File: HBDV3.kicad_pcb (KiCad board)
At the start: 2 copper layers, 56 parts, among them J1 RJ45 PWR, J2 Screw_Terminal_01x02 PWR, J3 RJ45 IN, J4 RJ45 OUT, J5 push_Terminal_01x04, J6 push_Terminal_01x04

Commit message: Changed diode, rough PCB layout
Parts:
- added H1: MountingHole, MountingHole:MountingHole_4.3mm_M4_DIN965, F.Cu at (165.0, 57.5)
- added H2: MountingHole, MountingHole:MountingHole_4.3mm_M4_DIN965, F.Cu at (225.0, 57.5)
- added H3: MountingHole, MountingHole:MountingHole_4.3mm_M4_DIN965, F.Cu at (211.0, 85.8)
- added H4: MountingHole, MountingHole:MountingHole_4.3mm_M4_DIN965, F.Cu at (251.0, 85.8)
- added J2: RJ45 PWR, Library:RJ45_E5J8800LJG2L, F.Cu at (150.8, 83.6)
- D1, D2, D3, D6, D7, D8: value QH05BZ600 -> PMEG10020ELRX; footprint Package_TO_SOT_SMD:TO-263-2 -> Diode_SMD:Nexperia_CFP3_SOD-123W
- moved J1 178.2 mm to (269.4, 88.3), turned to 90 degrees
- moved D7 174.7 mm to (250.1, 68.2)
- moved J4 174.7 mm to (269.1, 61.9), turned to 180 degrees
- moved D8 157.7 mm to (234.9, 93.7), turned to -90 degrees
- moved D6 152.2 mm to (229.8, 72.5)
- moved C8 137.9 mm to (275.8, 75.0), turned to 180 degrees
- moved C9 137.5 mm to (269.2, 72.8), turned to -90 degrees
- moved R24 135.6 mm to (266.2, 75.0), turned to 90 degrees
- moved R21 133.4 mm to (257.8, 74.8), turned to 90 degrees
- moved R18 132.4 mm to (242.2, 74.8), turned to 90 degrees
- moved R20 127.7 mm to (252.8, 74.8), turned to 90 degrees
- moved R17 124.3 mm to (236.8, 79.0), turned to 90 degrees
- moved R19 121.7 mm to (247.5, 74.8), turned to 90 degrees
- moved D10 118.9 mm to (262.5, 75.0), turned to 90 degrees
- moved R16 118.2 mm to (231.8, 79.0), turned to 90 degrees
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- renumbered J2 to J3, J3 to J4, J4 to J5, J5 to J6, J6 to J7
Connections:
- D1 pad 1: /VDDA -> Net-(D1-K)
- D1 pad 2: unconnected-(D1-NC-Pad2) -> /VOUTA
- D2 pad 1: Net-(D2-C) -> Net-(D2-K)
- D2 pad 2: unconnected-(D2-NC-Pad2) -> /VOUTB
- D3 pad 1: Net-(D3-C) -> /VDDA
- D3 pad 2: unconnected-(D3-NC-Pad2) -> Net-(D3-A)
- D6 pad 1: /VDDA_B -> Net-(D6-K)
- D6 pad 2: unconnected-(D6-NC-Pad2) -> /VOUTA_B
- D7 pad 1: Net-(D7-C) -> Net-(D7-K)
- D7 pad 2: unconnected-(D7-NC-Pad2) -> /VOUTB_B
- D8 pad 1: Net-(D8-C) -> /VDDA_B
- D8 pad 2: unconnected-(D8-NC-Pad2) -> Net-(D8-A)
- R10 pad 2: Net-(D1-A) -> Net-(D3-A)
- R14 pad 2: Net-(D7-C) -> Net-(D6-K)
- R15 pad 2: Net-(D7-C) -> Net-(D6-K)
- R18 pad 2: Net-(D8-C) -> Net-(D7-K)
- R19 pad 2: Net-(D8-C) -> Net-(D7-K)
- R2 pad 2: Net-(D2-C) -> Net-(D1-K)
- R22 pad 2: Net-(D6-A) -> Net-(D8-A)
- R3 pad 2: Net-(D2-C) -> Net-(D1-K)
- R6 pad 2: Net-(D3-C) -> Net-(D2-K)
- R7 pad 2: Net-(D3-C) -> Net-(D2-K)
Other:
- board outline added: 137 x 45 mm

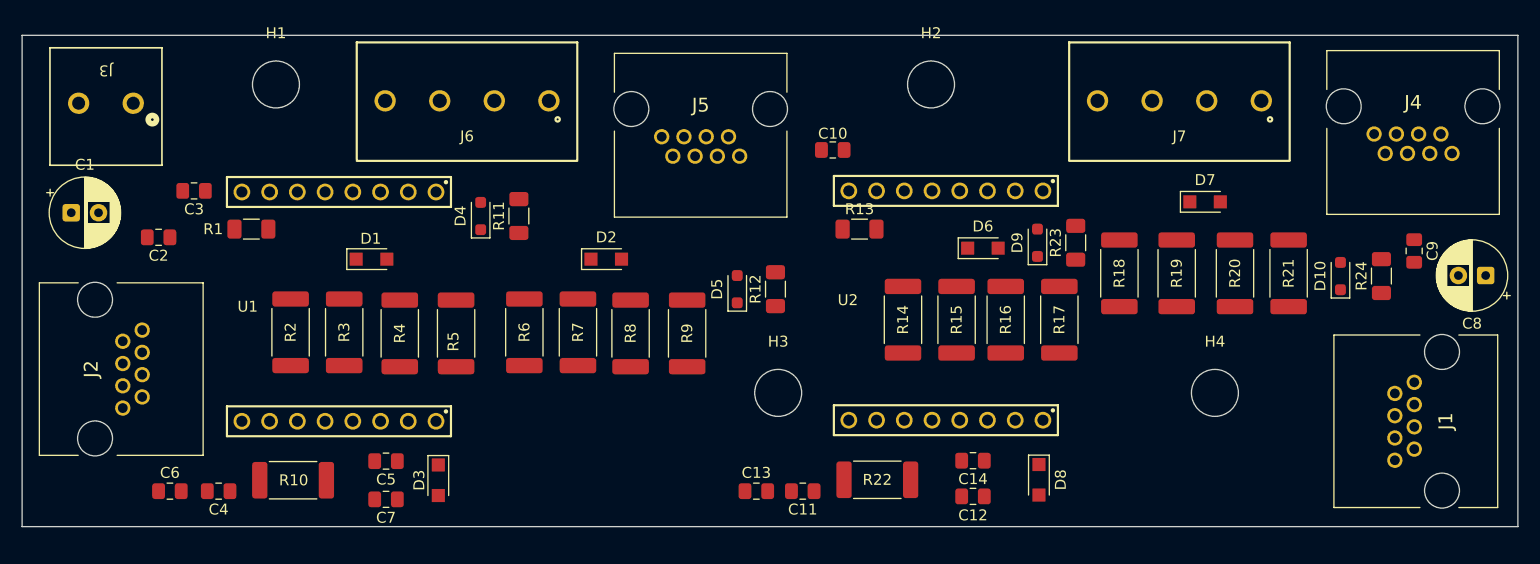
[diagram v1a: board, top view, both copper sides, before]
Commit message: Finished layout, added silkscreen text, configured track width
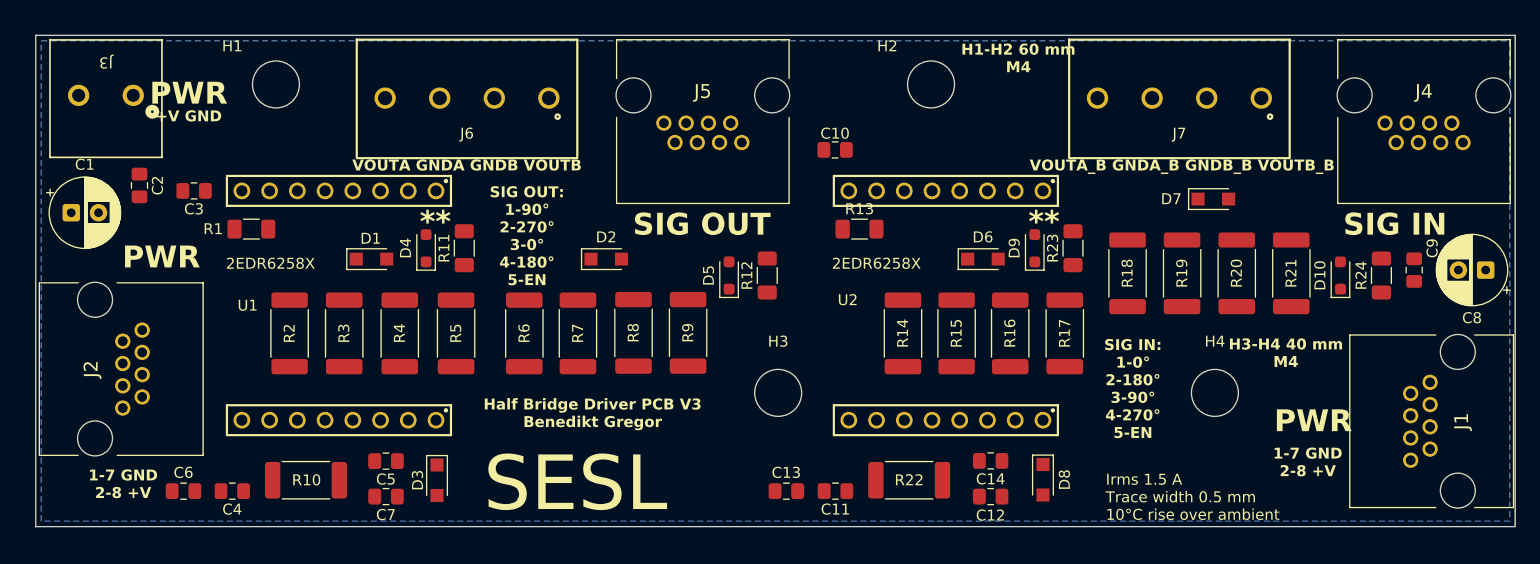
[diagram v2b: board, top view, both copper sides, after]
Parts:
- moved D4 5.81 mm to (178.8, 72.5)
- moved R11 5.81 mm to (182.2, 72.5)
- moved C2 5.06 mm to (152.5, 66.8), turned to -90 degrees
- moved C11 3.00 mm to (216.2, 94.8)
- moved R22 2.92 mm to (223.0, 93.8)
- moved C13 2.75 mm to (211.8, 94.8)
- moved C9 1.75 mm to (269.2, 74.5)
- moved C12 1.62 mm to (230.5, 95.2)
- moved C14 1.62 mm to (230.5, 92.0)
- moved D5 1.46 mm to (206.5, 75.0)
- moved R12 1.46 mm to (210.0, 75.0)
- moved J1 1.45 mm to (270.9, 88.3)
- moved J4 1.41 mm to (270.1, 60.9)
- moved R17 1.35 mm to (237.2, 80.3)
- moved R16 1.32 mm to (232.2, 80.3)
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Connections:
- net Net-(U1-STP/DTC) renamed /STP U1
- net Net-(U2-STP/DTC) renamed /STP U2
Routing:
- added copper zone on B.Cu, net GND
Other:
- board size 137 x 45 mm -> 135.5 x 45 mm
- board text added: "**"
- board text added: "+V GND"
- board text added: "1-7 GND 2-8 +V"
- board text added: "2EDR6258X"
- board text added: "H1-H2 60 mm M4"
- board text added: "H3-H4 40 mm M4"
- board text added: "Half Bridge Driver PCB V3 Benedikt Gregor"
- board text added: "Irms 1.5 A Trace width 0.5 mm 10°C rise over ambient"
- board text added: "PWR"
- board text added: "SESL"
- board text added: "SIG IN"
- board text added: "SIG IN: 1-0° 2-180° 3-90° 4-270° 5-EN"
- board text added: "SIG OUT"
- board text added: "SIG OUT: 1-90° 2-270° 3-0° 4-180° 5-EN"
- board text added: "VOUTA GNDA GNDB VOUTB"
- board text added: "VOUTA_B GNDA_B GNDB_B VOUTB_B"

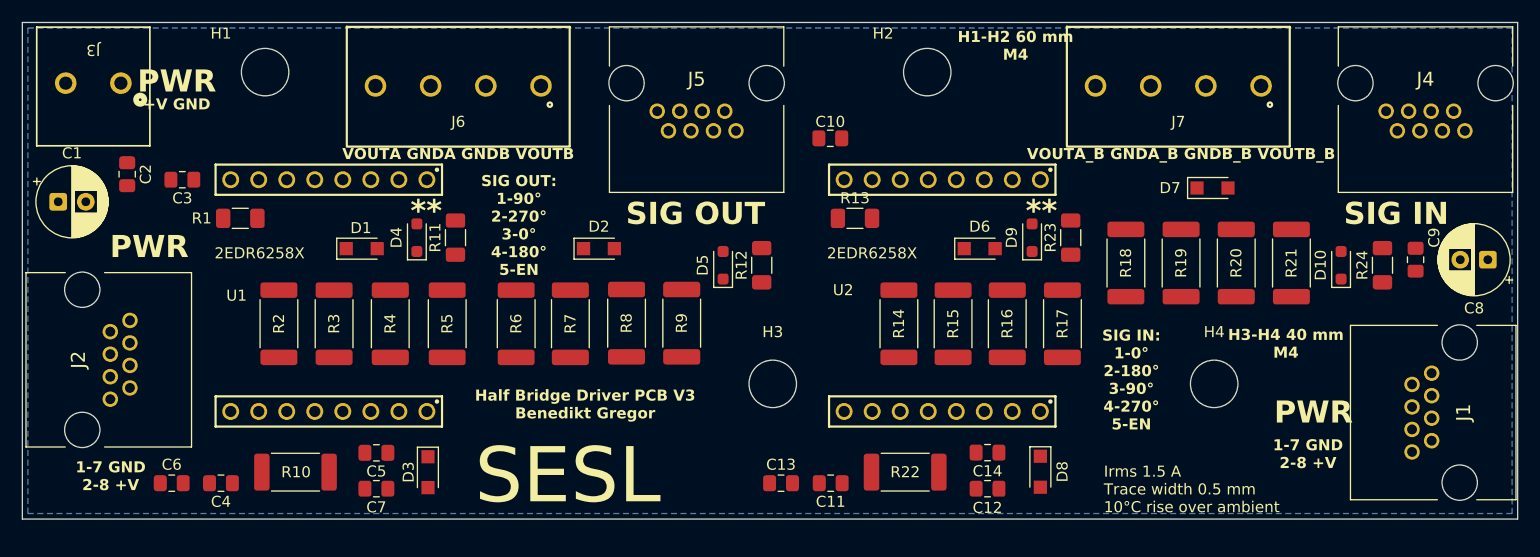
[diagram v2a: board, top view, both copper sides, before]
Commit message: Finished PCB routing
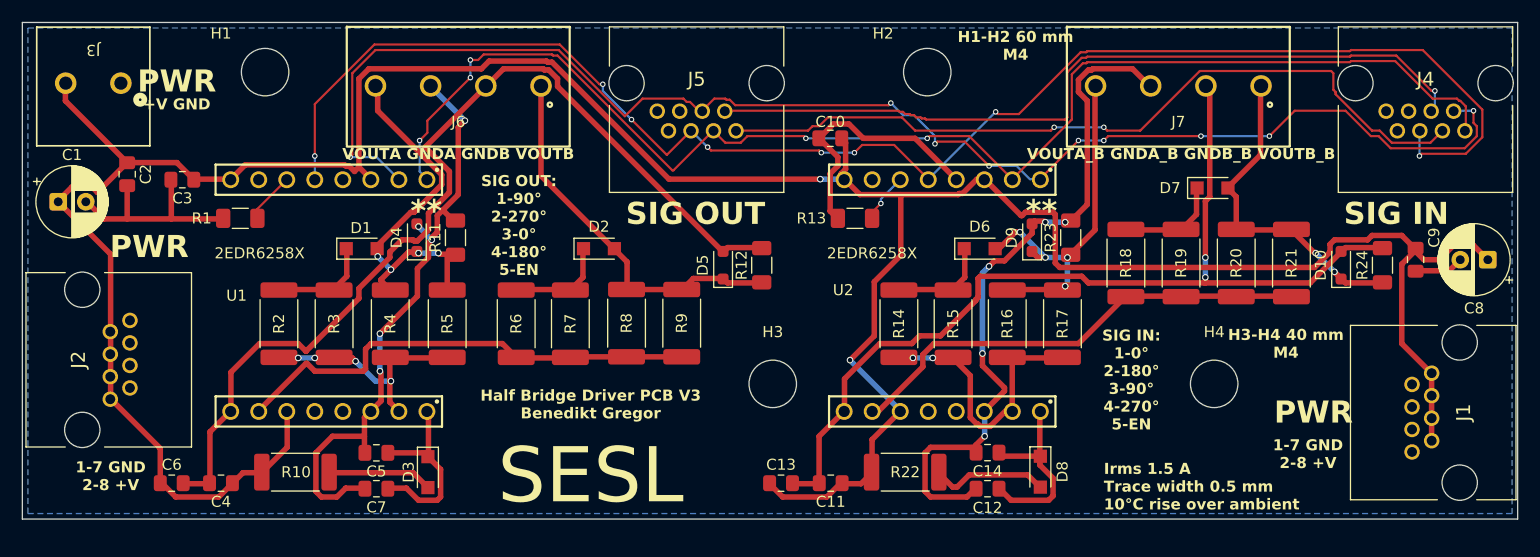
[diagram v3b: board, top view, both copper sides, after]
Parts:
- added G***: LOGO, LOGO, B.Cu at (193.5, 76.8)
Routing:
- net +16.5V: track 0.00 -> 279.1 mm, vias 0 -> 2
- net /ENABLE: track 0.00 -> 141.1 mm, vias 0 -> 8
- net Phase 180: track 0.00 -> 131.9 mm, vias 0 -> 9
- net Phase 0: track 0.00 -> 122.4 mm, vias 0 -> 5
- net /GNDB: track 0.00 -> 88.3 mm
- net /GNDB_B: track 0.00 -> 86.4 mm, vias 0 -> 2
- net Phase 270: track 0.00 -> 72.8 mm, vias 0 -> 1
- net Phase 90: track 0.00 -> 71.6 mm, vias 0 -> 2
- net /GNDA_B: track 0.00 -> 63.5 mm, vias 0 -> 5
- net /GNDA: track 0.00 -> 55.3 mm, vias 0 -> 5
- net GND: track 0.00 -> 48.2 mm
- net /OUTB: track 0.00 -> 43.4 mm
- net /OUTB_B: track 0.00 -> 43.2 mm
- net /VOUTB: track 0.00 -> 34.7 mm
- net /VOUTA_B: track 0.00 -> 34.4 mm, vias 0 -> 4
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
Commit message: Updated sig in/out for phase splitter compatibility + zener series R
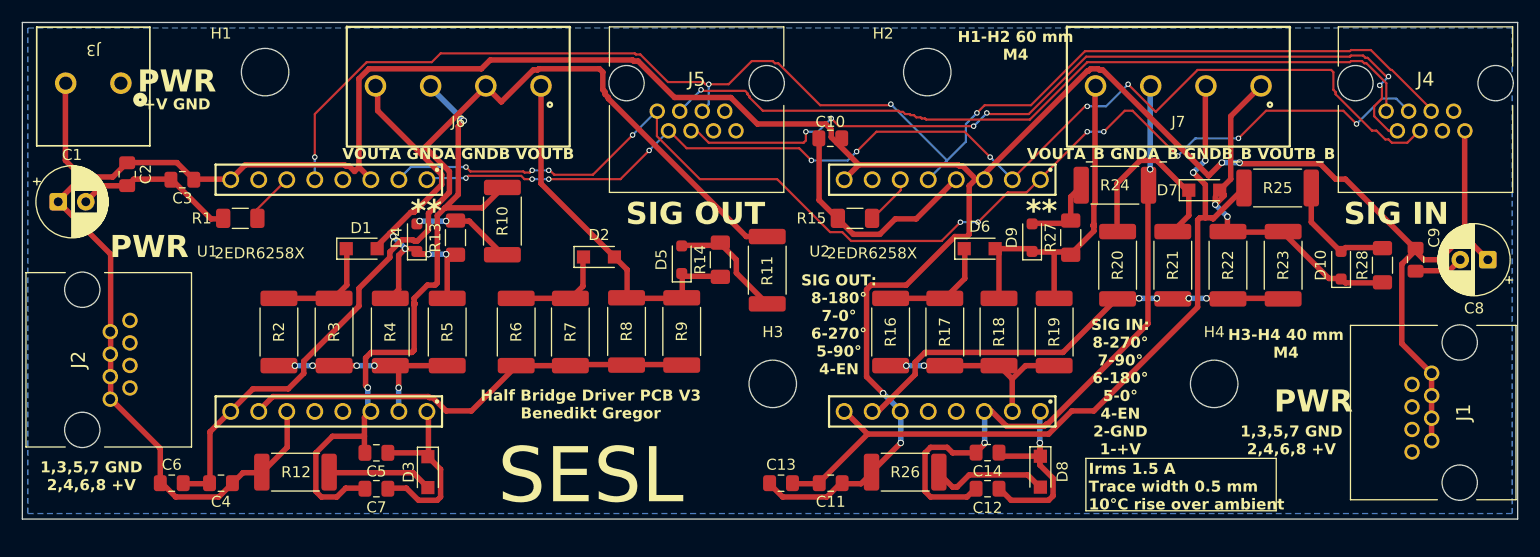
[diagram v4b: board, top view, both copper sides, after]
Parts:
- added R10: 2, Resistor_SMD:R_2512_6332Metric_Pad1.40x3.35mm_HandSolder, F.Cu at (186.5, 71.0)
- added R11: 2, Resistor_SMD:R_2512_6332Metric_Pad1.40x3.35mm_HandSolder, F.Cu at (210.5, 75.5)
- added R24: 2, Resistor_SMD:R_2512_6332Metric_Pad1.40x3.35mm_HandSolder, F.Cu at (242.0, 67.8)
- added R25: 2, Resistor_SMD:R_2512_6332Metric_Pad1.40x3.35mm_HandSolder, F.Cu at (256.8, 68.0)
- moved D5 3.78 mm to (202.8, 74.5)
- moved R14 3.78 mm to (206.2, 74.5)
- moved R16 1.06 mm to (221.7, 81.0)
- moved R17 1.06 mm to (226.6, 81.0)
- moved R18 1.06 mm to (231.5, 81.0)
- moved R19 1.06 mm to (236.5, 81.0)
- moved D7 0.78 mm to (250.1, 68.2)
- moved R20 0.78 mm to (242.2, 75.0)
- moved R21 0.78 mm to (247.2, 75.0)
- moved R22 0.78 mm to (252.2, 75.0)
- moved R23 0.78 mm to (257.2, 75.0)
- moved D2 0.75 mm to (195.2, 74.2)
- moved R2 0.75 mm to (166.2, 81.0)
- moved R3 0.75 mm to (171.2, 81.0)
- moved R4 0.75 mm to (176.3, 81.0)
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- renumbered R10 to R12, R11 to R13, R12 to R14, R13 to R15, R14 to R16, R15 to R17, R16 to R18, R17 to R19, R18 to R20, R19 to R21, R20 to R22, R21 to R23, R22 to R26, R23 to R27, R24 to R28
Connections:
- D10 pad 2: /GNDB_B -> Net-(D10-A)
- D4 pad 2: /GNDA -> Net-(D4-A)
- D5 pad 2: /GNDB -> Net-(D5-A)
- D9 pad 2: /GNDA_B -> Net-(D9-A)
- J4 pad 1: Phase 0 -> +16.5V
- J4 pad 2: Phase 180 -> GND
- J4 pad 3: Phase 90 -> unconnected-(J4-Pad3)
- J4 pad 4: Phase 270 -> /ENABLE
- J4 pad 5: /ENABLE -> Phase 0
- J4 pad 6: unconnected-(J4-Pad6) -> Phase 180
- J4 pad 7: unconnected-(J4-Pad7) -> Phase 90
- J4 pad 8: unconnected-(J4-Pad8) -> Phase 270
- J5 pad 1: Phase 90 -> unconnected-(J5-Pad1)
- J5 pad 2: Phase 270 -> unconnected-(J5-Pad2)
- J5 pad 3: Phase 0 -> unconnected-(J5-Pad3)
- J5 pad 4: Phase 180 -> /ENABLE
- J5 pad 5: /ENABLE -> Phase 90
- J5 pad 6: unconnected-(J5-Pad6) -> Phase 270
- J5 pad 7: unconnected-(J5-Pad7) -> Phase 0
- J5 pad 8: unconnected-(J5-Pad8) -> Phase 180
- R13 pad 2: /GNDA -> Net-(D4-A)
- R14 pad 2: /GNDB -> Net-(D5-A)
- R27 pad 2: /GNDA_B -> Net-(D9-A)
- R28 pad 2: /GNDB_B -> Net-(D10-A)
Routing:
- net Phase 180: track 131.9 -> 111.1 mm, vias 9 -> 11
- net Phase 0: track 122.4 -> 106.2 mm, vias 5 -> 9
- net +16.5V: track 279.1 -> 294.8 mm, vias 2 -> 4
- net /GNDB_B: track 86.4 -> 72.7 mm
- net /ENABLE: track 141.1 -> 127.6 mm, vias 8 -> 4
- net Net-(D5-A): track 0.00 -> 10.9 mm
- net Net-(D10-A): track 0.00 -> 10.9 mm
- net Net-(D4-A): track 0.00 -> 9.22 mm, vias 0 -> 2
- net Net-(D7-K): track 9.53 -> 17.5 mm
- net Net-(D9-A): track 0.00 -> 7.37 mm
- net GND: track 48.2 -> 41.0 mm
- net /OUTA_B: track 26.1 -> 18.9 mm
- net /GNDA: track 55.3 -> 60.7 mm, vias 5 -> 2
- net /GNDA_B: track 63.5 -> 58.7 mm, vias 5 -> 2
- net Phase 90: track 71.6 -> 75.8 mm, vias 2 -> 6
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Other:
- board text added: "1,3,5,7 GND 2,4,6,8 +V"
- board text added: "SIG IN: 8-270° 7-90° 6-180° 5-0° 4-EN 2-GND 1-+V"
- board text added: "SIG OUT: 8-180° 7-0° 6-270° 5-90° 4-EN"
- board text removed: "1-7 GND 2-8 +V"
- board text removed: "SIG IN: 1-0° 2-180° 3-90° 4-270° 5-EN"
- board text removed: "SIG OUT: 1-90° 2-270° 3-0° 4-180° 5-EN"

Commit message: Gerber files and 4.7uF cap adjustment
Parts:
- C11, C12, C4, C5: value 2.2uF -> 4.7uF
- moved G*** 2.47 mm to (193.2, 79.2)
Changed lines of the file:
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@@
 			(plot_on_all_layers_selection 0x00000000_00000000_00000000_00000000)
 			(disableapertmacros no)
-			(usegerberextensions no)
+			(usegerberextensions yes)
 			(usegerberattributes yes)
 			(usegerberadvancedattributes yes)
-			(creategerberjobfile yes)
+			(creategerberjobfile no)
 			(dashed_line_dash_ratio 12)
 			(dashed_line_gap_ratio 3)
@@
 			(outputformat 1)
 			(mirror no)
-			(drillshape 1)
+			(drillshape 0)
 			(scaleselection 1)
-			(outputdirectory "")
+			(outputdirectory "Gerberfiles_jlc")
 		)
 	)
@@
 			)
 		)
-		(property "Value" "2.2uF"
+		(property "Value" "4.7uF"
 			(at 0 1.68 0)
 			(layer "F.Fab")
@@
 			)
 		)
-		(property "Value" "2.2uF"
+		(property "Value" "4.7uF"
 			(at 0 1.68 0)
 			(layer "F.Fab")
@@
 			)
 		)
-		(property "Value" "2.2uF"
+		(property "Value" "4.7uF"
 			(at 0 1.68 0)
 			(layer "F.Fab")
@@
 			)
 		)
-		(property "Value" "2.2uF"
+		(property "Value" "4.7uF"
 			(at 0 1.68 0)
 			(layer "F.Fab")
@@
 	(footprint "LOGO"
 		(layer "B.Cu")
-		(at 193.5 76.75 180)
+		(at 193.225 79.2 180)
 		(property "Reference" "G***"
 			(at 0 0 0)
